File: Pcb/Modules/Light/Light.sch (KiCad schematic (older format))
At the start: 13 parts, among them J1 JACK_RJ45, J2 JACK_STEREO, Q1 TEPT4400, Q2 MMBT2907ALT1G, X1 HOLE, X2 HOLE, X3 HOLE, X4 HOLE

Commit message: Updated light module to new 2" x .8" board size with rounded corners.  Updated pot to RK09K series (lower cost), corrected 10uF C1 footprint size to 1206,  Added RK09K pot to CA6 footprint library.
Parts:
- removed X1, X2, X3, X4: HOLE, Mounting_Holes:MountingHole_2.2mm_M2, symbol HOLE
- RV1: footprint Potentiometers:Potentiometer_Alps_RK09L_Single_Vertical -> Potentiometers:Potentiometer_Alps_RK09K_Vertical
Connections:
- wire segments 21 -> 22
- no-connect marks 4 -> 5
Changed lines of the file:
@@
 EESchema Schematic File Version 2
 LIBS:CA6
+LIBS:74xx
 LIBS:74xgxx
-LIBS:74xx
 LIBS:ac-dc
 LIBS:actel
@@
 LIBS:battery_management
 LIBS:bbd
-LIBS:bosch
 LIBS:brooktre
 LIBS:cmos_ieee
@@
 LIBS:ir
 LIBS:Lattice
-LIBS:leds
 LIBS:linear
 LIBS:logo
@@
 LIBS:microchip_pic16mcu
 LIBS:microchip_pic18mcu
-LIBS:microchip_pic24mcu
 LIBS:microchip_pic32mcu
 LIBS:microcontrollers
-LIBS:modules
 LIBS:motor_drivers
 LIBS:motorola
@@
 LIBS:msp430
 LIBS:nordicsemi
-LIBS:nxp
 LIBS:nxp_armmcu
 LIBS:onsemi
@@
 LIBS:transf
 LIBS:transistors
-LIBS:triac_thyristor
 LIBS:ttl_ieee
 LIBS:valves
@@
 LIBS:zetex
 LIBS:Zilog
-LIBS:light-sensor-cache
+LIBS:Light-cache
 EELAYER 25 0
 EELAYER END
@@
 F 0 "RV1" H 5900 3700 50  0000 C CNN
 F 1 "20K" V 5750 3600 50  0000 C CNN
-F 2 "Potentiometers:Potentiometer_Alps_RK09L_Single_Vertical" H 5750 3600 60  0001 C CNN
-F 3 "http://www.mouser.com/ProductDetail/ALPS/RK09L1120A2S/?qs=sGAEpiMZZMtC25l1F4XBUyOcKw5CnqLBtmCjw0rP5%252bQ%3d" H 5750 3600 60  0001 C CNN
+F 2 "Potentiometers:Potentiometer_Alps_RK09K_Vertical" H 5750 3600 591 0001 C CNN
+F 3 "http://www.mouser.com/ProductDetail/ALPS/RK09K1110AH8/?qs=sGAEpiMZZMtC25l1F4XBU3JeeCo7XMTlexI3BEsH1y4%3d" H 5750 3600 60  0001 C CNN
 	1    5750 3600
 	1    0    0    -1
@@
 Text Notes 5900 4100 0    39   ~ 0
 Choose R2 for MAX current of 20mA\n180 = 18.3 mA\n174 = 18.9 mA\n169 = 19.5 mA
-$Comp
-L HOLE X4
-U 1 1 590FF942
-P 4000 3000
-F 0 "X4" H 4000 2900 60  0000 C CNN
-F 1 "HOLE" H 4000 3100 60  0000 C CNN
-F 2 "Mounting_Holes:MountingHole_2.2mm_M2" H 4000 3000 60  0001 C CNN
-F 3 "" H 4000 3000 60  0000 C CNN
-	1    4000 3000
-	1    0    0    -1
-$EndComp
-$Comp
-L HOLE X2
-U 1 1 590FF985
-P 3750 3000
-F 0 "X2" H 3750 2900 60  0000 C CNN
-F 1 "HOLE" H 3750 3100 60  0000 C CNN
-F 2 "Mounting_Holes:MountingHole_2.2mm_M2" H 3750 3000 60  0001 C CNN
-F 3 "" H 3750 3000 60  0000 C CNN
-	1    3750 3000
-	1    0    0    -1
-$EndComp
-$Comp
-L HOLE X3
-U 1 1 590FF9D5
-P 4000 2650
-F 0 "X3" H 4000 2550 60  0000 C CNN
-F 1 "HOLE" H 4000 2750 60  0000 C CNN
-F 2 "Mounting_Holes:MountingHole_2.2mm_M2" H 4000 2650 60  0001 C CNN
-F 3 "" H 4000 2650 60  0000 C CNN
-	1    4000 2650
-	1    0    0    -1
-$EndComp
-$Comp
-L HOLE X1
-U 1 1 590FFA2B
-P 3750 2650
-F 0 "X1" H 3750 2550 60  0000 C CNN
-F 1 "HOLE" H 3750 2750 60  0000 C CNN
-F 2 "Mounting_Holes:MountingHole_2.2mm_M2" H 3750 2650 60  0001 C CNN
-F 3 "" H 3750 2650 60  0000 C CNN
-	1    3750 2650
-	1    0    0    -1
-$EndComp
+NoConn ~ 4650 3700
+$Comp
+L PWR_FLAG #FLG010
+U 1 1 59E23186
+P 4200 4350
+F 0 "#FLG010" H 4200 4425 50  0001 C CNN
+F 1 "PWR_FLAG" H 4200 4500 50  0000 C CNN
+F 2 "" H 4200 4350 50  0001 C CNN
+F 3 "" H 4200 4350 50  0001 C CNN
+	1    4200 4350
+	1    0    0    -1
+$EndComp
+$Comp
+L GND #PWR011
+U 1 1 59E231B3
+P 4200 4450
+F 0 "#PWR011" H 4200 4450 30  0001 C CNN
+F 1 "GND" H 4200 4380 30  0001 C CNN
+F 2 "" H 4200 4450 60  0000 C CNN
+F 3 "" H 4200 4450 60  0000 C CNN
+	1    4200 4450
+	1    0    0    -1
+$EndComp
+Wire Wire Line
+	4200 4350 4200 4450
 $EndSCHEMATC

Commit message: Fix some issues with dev module and cleanup light module
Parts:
- removed Q2: MMBT2907ALT1G, TO_SOT_Packages_SMD:SOT-23, symbol MMBT2907ALT1G
- added Q2: Q_NMOS_GSD, TO_SOT_Packages_SMD:SOT-23, symbol Q_NMOS_GSD
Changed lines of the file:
@@
 LIBS:zetex
 LIBS:Zilog
-LIBS:Light-cache
 EELAYER 25 0
 EELAYER END
@@
 Wire Wire Line
 	6550 5050 6500 5050
-$Comp
-L MMBT2907ALT1G Q2
-U 1 1 58FFB097
-P 6450 4600
-F 0 "Q2" H 6650 4500 50  0000 C CNN
-F 1 "MMBT2907ALT1G" V 6750 4650 50  0000 C CNN
-F 2 "TO_SOT_Packages_SMD:SOT-23" H 6450 4600 60  0001 C CNN
-F 3 "" H 6450 4600 60  0000 C CNN
-	1    6450 4600
-	1    0    0    1
-$EndComp
 Wire Wire Line
 	5550 4600 5400 4600
@@
 Wire Wire Line
 	4200 4350 4200 4450
+$Comp
+L Q_NMOS_GSD Q2
+U 1 1 59E3F4ED
+P 6450 4600
+F 0 "Q2" H 6650 4650 50  0000 L CNN
+F 1 "Q_NMOS_GSD" H 6650 4550 50  0001 L CNN
+F 2 "TO_SOT_Packages_SMD:SOT-23" H 6650 4700 50  0001 C CNN
+F 3 "" H 6450 4600 50  0000 C CNN
+	1    6450 4600
+	1    0    0    -1
+$EndComp
 $EndSCHEMATC

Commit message: Update pcbs
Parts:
- added MK1, MK2, MK3: Mounting_Hole, Mounting_Holes:MountingHole_2.5mm_Pad, symbol Mounting_Hole
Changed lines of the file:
@@
 LIBS:zetex
 LIBS:Zilog
+LIBS:Light-cache
 EELAYER 25 0
 EELAYER END
@@
 	1    0    0    -1
 $EndComp
+$Comp
+L Mounting_Hole MK1
+U 1 1 5A1F1815
+P 3200 3100
+F 0 "MK1" H 3200 3300 50  0000 C CNN
+F 1 "Mounting_Hole" H 3200 3225 50  0000 C CNN
+F 2 "Mounting_Holes:MountingHole_2.5mm_Pad" H 3200 3100 60  0001 C CNN
+F 3 "" H 3200 3100 60  0001 C CNN
+	1    3200 3100
+	1    0    0    -1
+$EndComp
+$Comp
+L Mounting_Hole MK2
+U 1 1 5A1F1870
+P 3200 3450
+F 0 "MK2" H 3200 3650 50  0000 C CNN
+F 1 "Mounting_Hole" H 3200 3575 50  0000 C CNN
+F 2 "Mounting_Holes:MountingHole_2.5mm_Pad" H 3200 3450 60  0001 C CNN
+F 3 "" H 3200 3450 60  0001 C CNN
+	1    3200 3450
+	1    0    0    -1
+$EndComp
+$Comp
+L Mounting_Hole MK3
+U 1 1 5A1F18E3
+P 3200 3800
+F 0 "MK3" H 3200 4000 50  0000 C CNN
+F 1 "Mounting_Hole" H 3200 3925 50  0000 C CNN
+F 2 "Mounting_Holes:MountingHole_2.5mm_Pad" H 3200 3800 60  0001 C CNN
+F 3 "" H 3200 3800 60  0001 C CNN
+	1    3200 3800
+	1    0    0    -1
+$EndComp

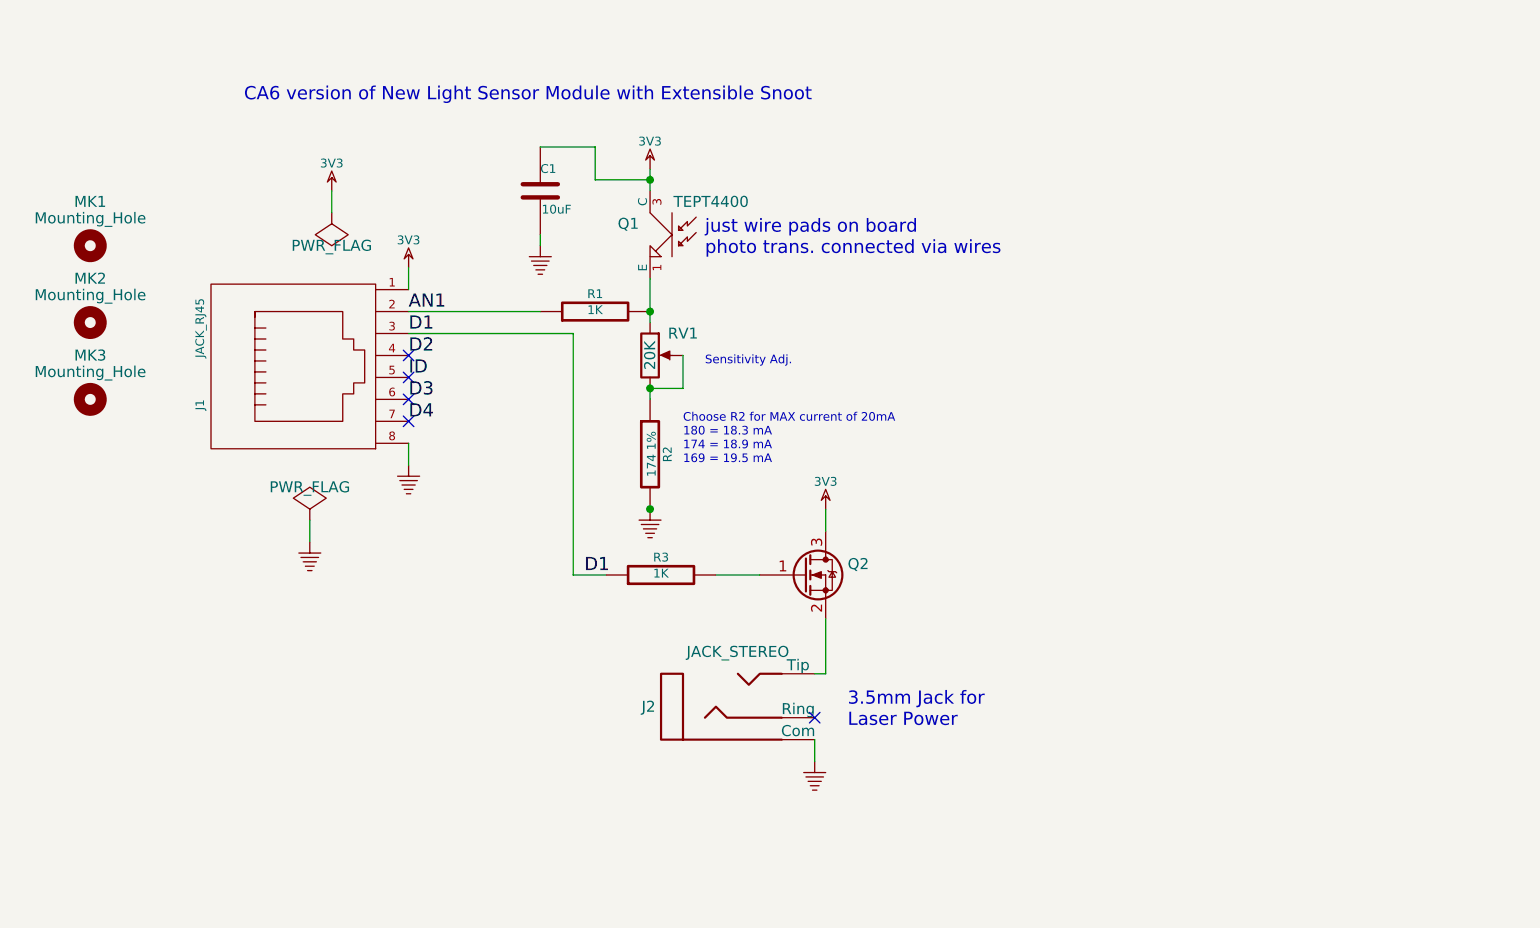
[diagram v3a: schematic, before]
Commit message: Updated the Schematic & PCB for the Light sensor to incorporate the new, auto-sensitivity circuit using two single-buffer chips and a resistor ladder instead of the pot.  The Values of R4 and R5 might still need to be optimized, but are workable.  R3 (160 ohm) was reduced to compensate for the voltage drop across buffer U1.  R3, 4, 5 use the 0603 footprint, but we should consider using a higher wattage version for R3 (160 ohm).  R3 @20 mA = 66mW, so a 1/10W version might be not enough headroom, but certainly the 200mW version would be fine.  R3 should be 1%.  The PCB is workable, but could certainly use better optimization of parts placement.
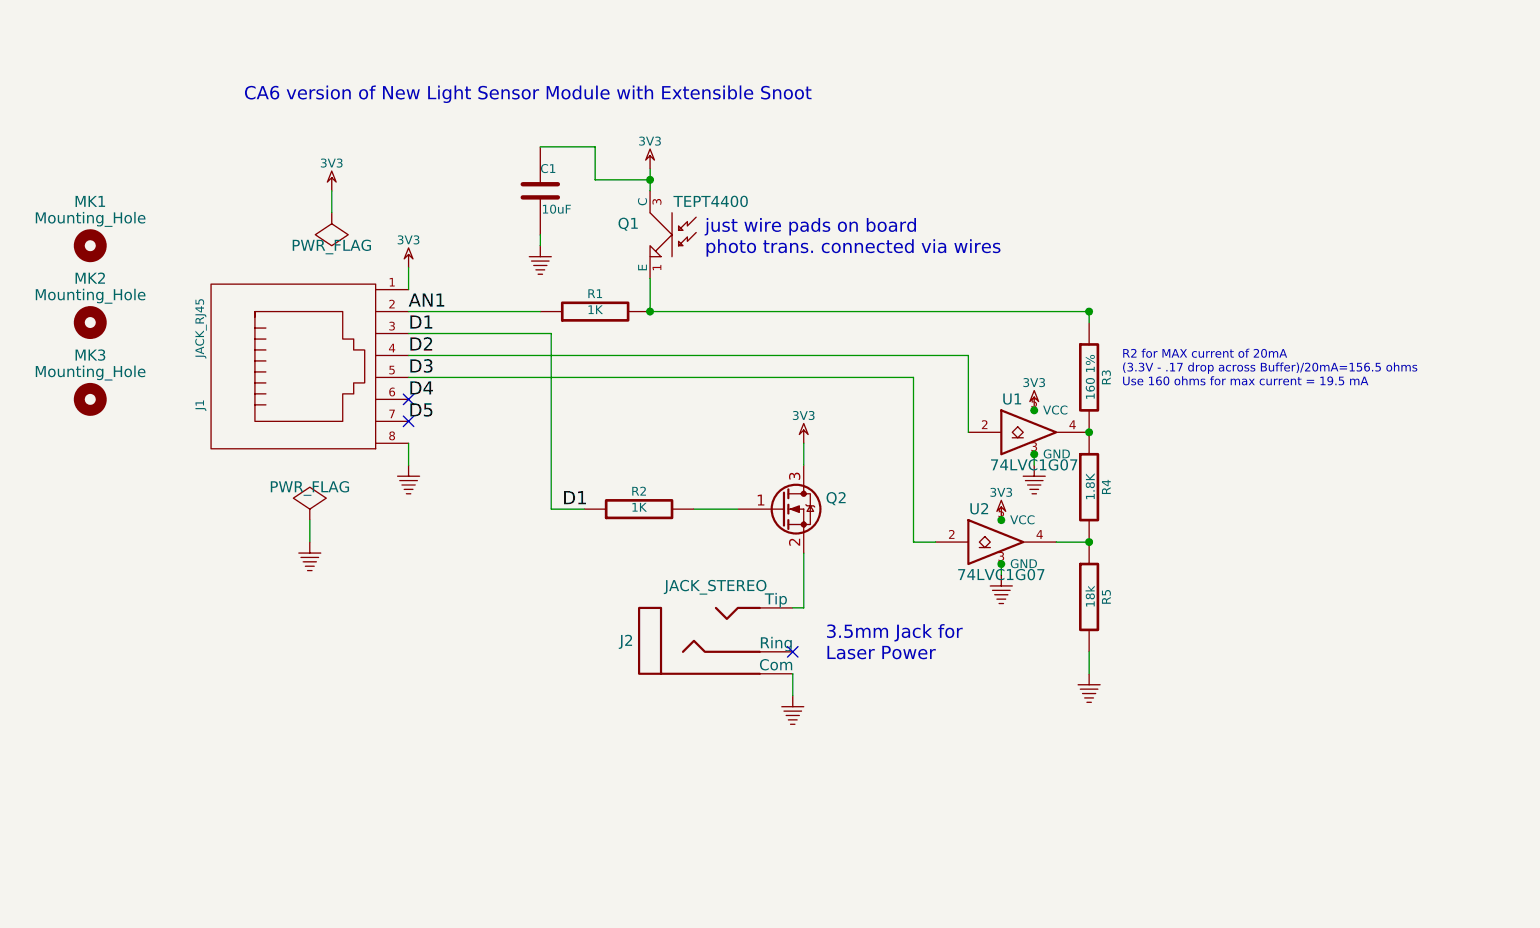
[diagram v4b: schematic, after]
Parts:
- removed RV1: 20K, Potentiometers:Potentiometer_Alps_RK09K_Vertical, symbol POT
- added R4: 1.8K, CA6:SM0603_Resistor, symbol R
- added R5: 18k, CA6:SM0603_Resistor, symbol R
- added U1, U2: 74LVC1G07, TO_SOT_Packages_SMD:SOT-353_SC-70-5, symbol 74LVC1G07
- R3: renamed from R2; value 174 1% -> 160 1%; footprint CA6:SM0805_Resistor -> CA6:SM0603_Resistor
- renumbered R3 to R2
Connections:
- net ID is gone; now on net D3: J1.5
- net 3V3: now also U1.5 (VCC), U2.5 (VCC)
- net D2: now also U1.2
- net D3: now also U2.2; no longer J1.6
- net D4: now also J1.6; no longer J1.7
- net GND: now also R5.2, U1.3 (GND), U2.3 (GND); no longer R3.2
- net at Q1.1 (E), R1.2: now also R3.1
- new net: R3.2, R4.1, U1.4
- new net: R4.2, R5.1, U2.4
- new net D5: J1.7
- no-connect marks 5 -> 3
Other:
- note added: "R2 for MAX current of 20mA\n(3.3V - .17 drop across Buffer)/20mA=156.5 ohms\nUse 160 ohms for max current = 19.5 mA"
- note removed: "Choose R2 for MAX current of 20mA\n180 = 18.3 mA\n174 = 18.9 mA\n169 = 19.5 mA"
- note removed: "Sensitivity Adj."
- moved on the sheet: J2, Q2, R2, R3

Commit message: Update light module
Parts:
- added C2: 100uF, CA6:c_elec_6.3x5.7, symbol CAP_ELEC
- added C3: 10uF, CA6:c_1206, symbol C
- MK1: footprint Mounting_Holes:MountingHole_2.5mm_Pad -> Mounting_Holes:MountingHole_4.5mm_Pad
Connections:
- net 3V3: now also C2.1, C3.1
- net GND: now also C2.2, C3.2
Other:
- moved on the sheet: J2, Q2, R2, R4, R5, U1, U2

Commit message: Update light pcb
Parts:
- R3: footprint CA6:SM0603_Resistor -> Resistors_SMD:R_1206
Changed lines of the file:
@@
 $EndComp
 $Comp
-L 3V3 #PWR3
+L 3V3 #PWR01
 U 1 1 540144B1
 P 4650 3200
-F 0 "#PWR3" H 4650 3300 40  0001 C CNN
+F 0 "#PWR01" H 4650 3300 40  0001 C CNN
 F 1 "3V3" H 4650 3325 40  0000 C CNN
 F 2 "" H 4650 3200 60  0000 C CNN
@@
 D5
 $Comp
-L GND #PWR4
+L GND #PWR02
 U 1 1 540144C2
 P 4650 4100
-F 0 "#PWR4" H 4650 4100 30  0001 C CNN
+F 0 "#PWR02" H 4650 4100 30  0001 C CNN
 F 1 "GND" H 4650 4030 30  0001 C CNN
 F 2 "" H 4650 4100 60  0000 C CNN
@@
 	4650 3200 4650 3300
 $Comp
-L 3V3 #PWR7
+L 3V3 #PWR03
 U 1 1 5401450D
 P 5800 3800
-F 0 "#PWR7" H 5800 3900 40  0001 C CNN
+F 0 "#PWR03" H 5800 3900 40  0001 C CNN
 F 1 "3V3" H 5800 3925 40  0000 C CNN
 F 2 "" H 5800 3800 60  0000 C CNN
@@
 $EndComp
 $Comp
-L GND #PWR8
+L GND #PWR04
 U 1 1 5401451B
 P 6400 5500
-F 0 "#PWR8" H 6400 5500 30  0001 C CNN
+F 0 "#PWR04" H 6400 5500 30  0001 C CNN
 F 1 "GND" H 6400 5430 30  0001 C CNN
 F 2 "" H 6400 5500 60  0000 C CNN
@@
 F 0 "R3" V 7830 3700 40  0000 C CNN
 F 1 "160 1%" V 7757 3701 40  0000 C CNN
-F 2 "CA6:SM0603_Resistor" V 7680 3700 30  0001 C CNN
-F 3 "http://www.mouser.com/ds/2/315/AOA0000C283-1093288.pdf" H 7750 3700 30  0001 C CNN
+F 2 "Resistors_SMD:R_1206" V 7680 3700 30  0001 C CNN
+F 3 "" H 7750 3700 30  0001 C CNN
 	1    7750 3700
 	1    0    0    -1
 $EndComp
 $Comp
-L 3V3 #PWR6
+L 3V3 #PWR05
 U 1 1 54AA199D
 P 5750 2750
-F 0 "#PWR6" H 5750 2850 40  0001 C CNN
+F 0 "#PWR05" H 5750 2850 40  0001 C CNN
 F 1 "3V3" H 5750 2875 40  0000 C CNN
 F 2 "" H 5750 2750 60  0000 C CNN
@@
 $EndComp
 $Comp
-L GND #PWR13
+L GND #PWR06
 U 1 1 54AA1A1B
 P 7750 5300
-F 0 "#PWR13" H 7750 5300 30  0001 C CNN
+F 0 "#PWR06" H 7750 5300 30  0001 C CNN
 F 1 "GND" H 7750 5230 30  0001 C CNN
 F 2 "" H 7750 5300 60  0000 C CNN
@@
 $EndComp
 $Comp
-L GND #PWR5
+L GND #PWR07
 U 1 1 54AABCE0
 P 5250 3100
-F 0 "#PWR5" H 5250 3100 30  0001 C CNN
+F 0 "#PWR07" H 5250 3100 30  0001 C CNN
 F 1 "GND" H 5250 3030 30  0001 C CNN
 F 2 "" H 5250 3100 60  0000 C CNN
@@
 NoConn ~ 6400 5300
 $Comp
-L PWR_FLAG #FLG2
+L PWR_FLAG #FLG08
 U 1 1 58FEFDE5
 P 4300 2950
-F 0 "#FLG2" H 4300 3025 50  0001 C CNN
+F 0 "#FLG08" H 4300 3025 50  0001 C CNN
 F 1 "PWR_FLAG" H 4300 3100 50  0000 C CNN
 F 2 "" H 4300 2950 50  0001 C CNN
@@
 $EndComp
 $Comp
-L 3V3 #PWR2
+L 3V3 #PWR09
 U 1 1 58FEFE63
 P 4300 2850
-F 0 "#PWR2" H 4300 2950 40  0001 C CNN
+F 0 "#PWR09" H 4300 2950 40  0001 C CNN
 F 1 "3V3" H 4300 2975 40  0000 C CNN
 F 2 "" H 4300 2850 60  0000 C CNN
@@
 R2 for MAX current of 20mA\n(3.3V - .17 drop across Buffer)/20mA=156.5 ohms\nUse 160 ohms for max current = 19.5 mA
 $Comp
-L PWR_FLAG #FLG1
+L PWR_FLAG #FLG010
 U 1 1 59E23186
 P 4200 4350
-F 0 "#FLG1" H 4200 4425 50  0001 C CNN
+F 0 "#FLG010" H 4200 4425 50  0001 C CNN
 F 1 "PWR_FLAG" H 4200 4500 50  0000 C CNN
 F 2 "" H 4200 4350 50  0001 C CNN
@@
 $EndComp
 $Comp
-L GND #PWR1
+L GND #PWR011
 U 1 1 59E231B3
 P 4200 4450
-F 0 "#PWR1" H 4200 4450 30  0001 C CNN
+F 0 "#PWR011" H 4200 4450 30  0001 C CNN
 F 1 "GND" H 4200 4380 30  0001 C CNN
 F 2 "" H 4200 4450 60  0000 C CNN
@@
 	6950 3700 4650 3700
 $Comp
-L GND #PWR10
+L GND #PWR012
 U 1 1 5A247E92
 P 7350 4850
-F 0 "#PWR10" H 7350 4850 30  0001 C CNN
+F 0 "#PWR012" H 7350 4850 30  0001 C CNN
 F 1 "GND" H 7350 4780 30  0001 C CNN
 F 2 "" H 7350 4850 60  0000 C CNN
@@
 $EndComp
 $Comp
-L GND #PWR12
+L GND #PWR013
 U 1 1 5A247ECA
 P 7500 4200
-F 0 "#PWR12" H 7500 4200 30  0001 C CNN
+F 0 "#PWR013" H 7500 4200 30  0001 C CNN
 F 1 "GND" H 7500 4130 30  0001 C CNN
 F 2 "" H 7500 4200 60  0000 C CNN
@@
 $EndComp
 $Comp
-L 3V3 #PWR11
+L 3V3 #PWR014
 U 1 1 5A248403
 P 7500 3800
-F 0 "#PWR11" H 7500 3900 40  0001 C CNN
+F 0 "#PWR014" H 7500 3900 40  0001 C CNN
 F 1 "3V3" H 7500 3925 40  0000 C CNN
 F 2 "" H 7500 3800 60  0000 C CNN
@@
 $EndComp
 $Comp
-L 3V3 #PWR9
+L 3V3 #PWR015
 U 1 1 5A2484A4
 P 7350 4400
-F 0 "#PWR9" H 7350 4500 40  0001 C CNN
+F 0 "#PWR015" H 7350 4500 40  0001 C CNN
 F 1 "3V3" H 7350 4550 40  0000 C CNN
 F 2 "" H 7350 4400 60  0000 C CNN
@@
 Connection ~ 5900 3800
 $Comp
-L GND #PWR?
+L GND #PWR016
 U 1 1 5A2880E8
 P 5900 4300
-F 0 "#PWR?" H 5900 4300 30  0001 C CNN
+F 0 "#PWR016" H 5900 4300 30  0001 C CNN
 F 1 "GND" H 5900 4230 30  0001 C CNN
 F 2 "" H 5900 4300 60  0000 C CNN
@@
 $EndComp
 $Comp
-L GND #PWR?
+L GND #PWR017
 U 1 1 5A288126
 P 6300 4300
-F 0 "#PWR?" H 6300 4300 30  0001 C CNN
+F 0 "#PWR017" H 6300 4300 30  0001 C CNN
 F 1 "GND" H 6300 4230 30  0001 C CNN
 F 2 "" H 6300 4300 60  0000 C CNN

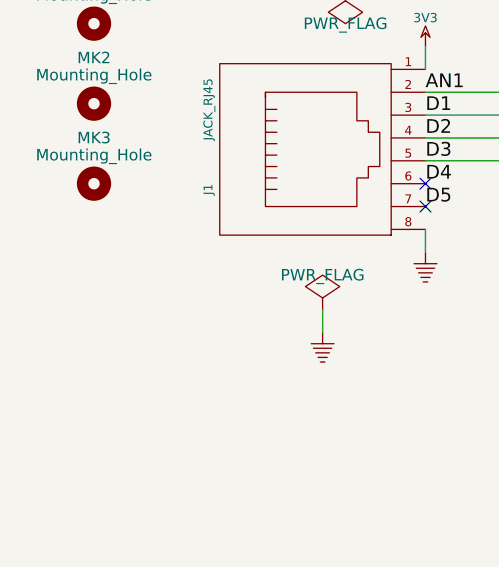
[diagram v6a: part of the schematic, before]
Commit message: Update light module to make PCB wider
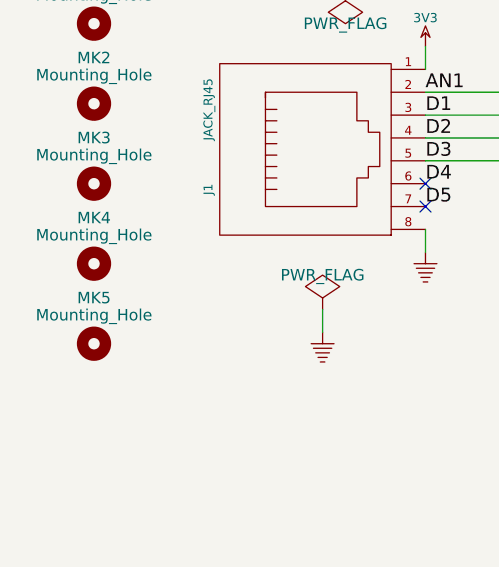
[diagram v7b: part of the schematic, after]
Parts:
- added MK4, MK5: Mounting_Hole, Mounting_Holes:MountingHole_2.5mm_Pad, symbol Mounting_Hole
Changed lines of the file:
@@
 Wire Wire Line
 	5900 4250 5900 4300
+$Comp
+L Mounting_Hole MK4
+U 1 1 5A2EE04A
+P 3200 4150
+F 0 "MK4" H 3200 4350 50  0000 C CNN
+F 1 "Mounting_Hole" H 3200 4275 50  0000 C CNN
+F 2 "Mounting_Holes:MountingHole_2.5mm_Pad" H 3200 4150 60  0001 C CNN
+F 3 "" H 3200 4150 60  0001 C CNN
+	1    3200 4150
+	1    0    0    -1
+$EndComp
+$Comp
+L Mounting_Hole MK5
+U 1 1 5A2EE142
+P 3200 4500
+F 0 "MK5" H 3200 4700 50  0000 C CNN
+F 1 "Mounting_Hole" H 3200 4625 50  0000 C CNN
+F 2 "Mounting_Holes:MountingHole_2.5mm_Pad" H 3200 4500 60  0001 C CNN
+F 3 "" H 3200 4500 60  0001 C CNN
+	1    3200 4500
+	1    0    0    -1
+$EndComp
 $EndSCHEMATC
